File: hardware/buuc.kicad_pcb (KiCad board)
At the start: 2 copper layers, 45.1 x 29.8 mm, 15 parts, among them P1 USB_OTG, P2 CONN_01X02, Q1 NDS8434, U1 BOOST_REGULATOR, U2 MCP73842-840I/UN

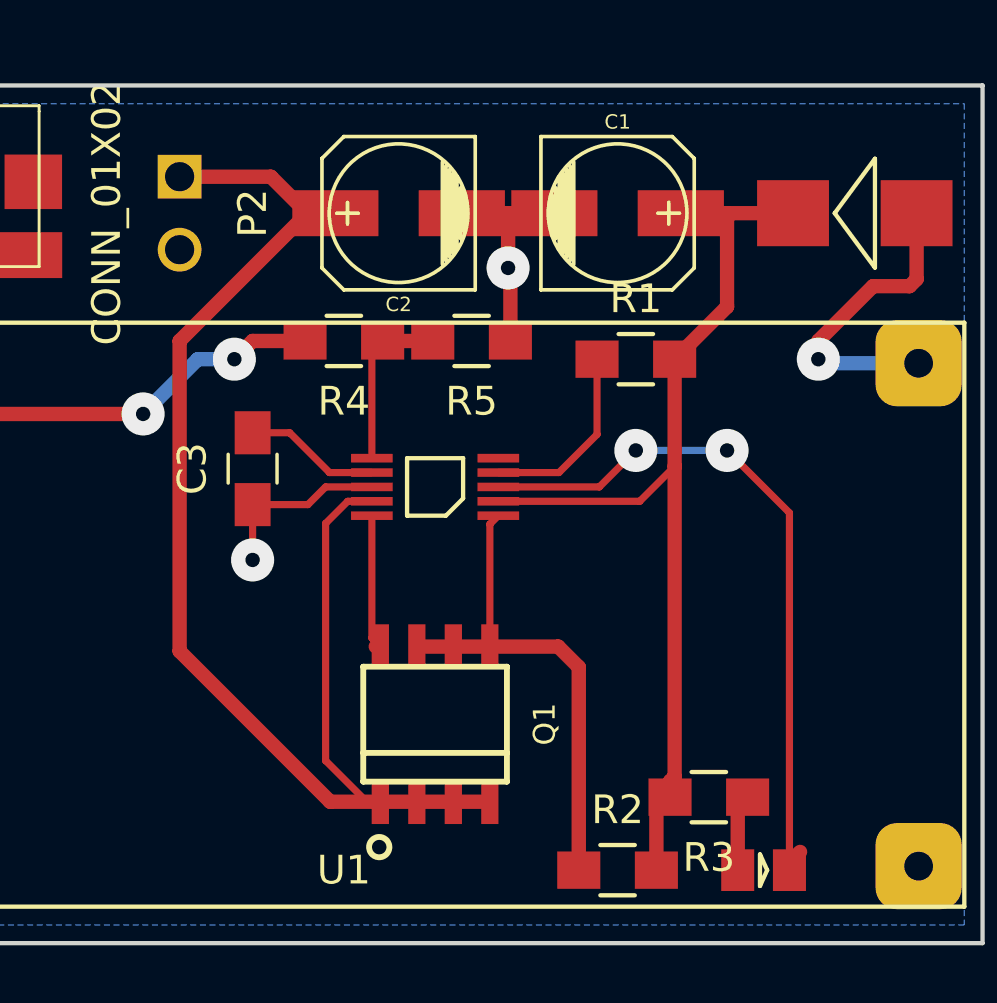
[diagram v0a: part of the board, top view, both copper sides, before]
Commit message: Updating schematics.
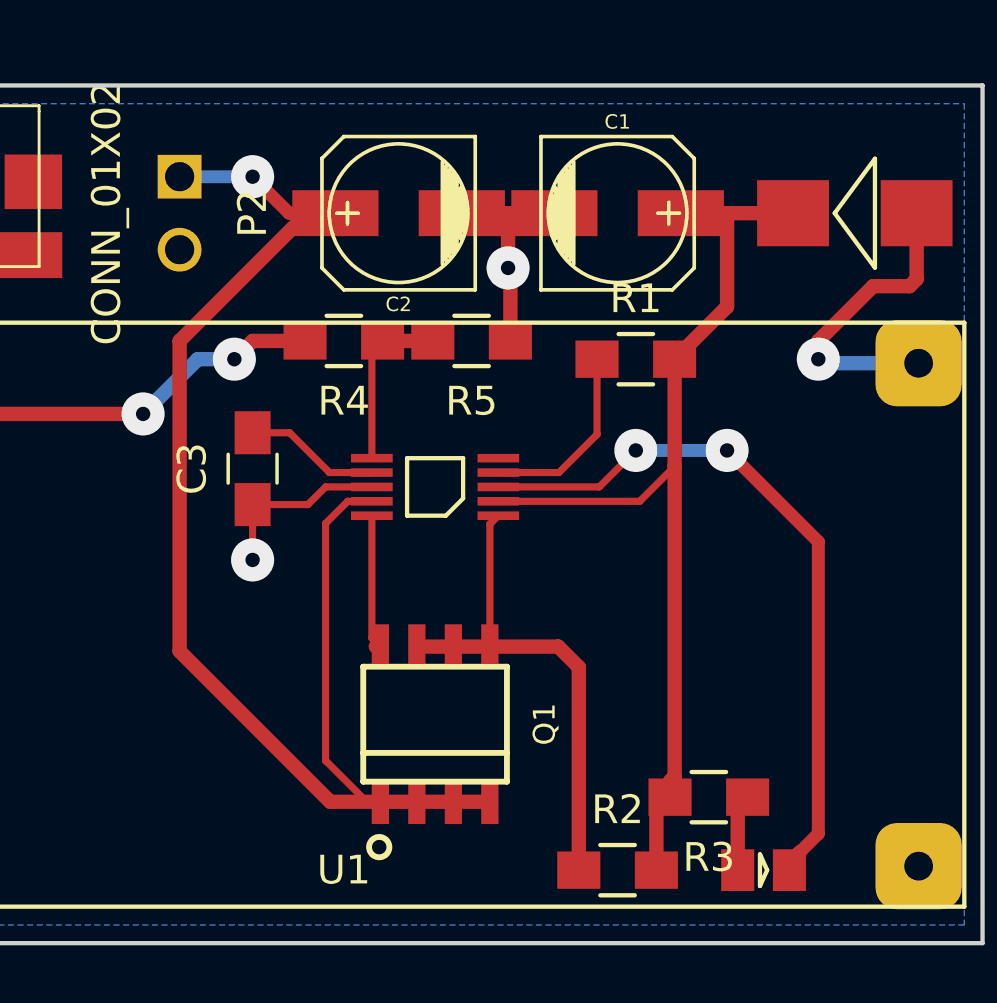
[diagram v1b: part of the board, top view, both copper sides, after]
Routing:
- net +BATT: track 49.6 -> 50.6 mm, vias 0 -> 1
- net Net-(D2-Pad1): track 24.8 -> 25.3 mm
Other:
- net class Default: trace_width 0.25 -> 0.45

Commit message: Adding MIC2005 current limiting IC; I haven't even soldered everything together, but it's pretty clear this will be necessary.
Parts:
- added C4: 0.1u, KiCad/Capacitors_SMD.pretty:C_0805_HandSoldering, F.Cu at (59.1, 48.3)
- added R6: 10k, apexelectrix/apex-smd-resistors.pretty:R_0805_HandSoldering, F.Cu at (57.1, 45.7)
- added U3: MIC2005A, adamgreig/agg-kicad/agg.pretty:SOT-23-6, F.Cu at (57.1, 54.0)
- moved C1 90.5 mm to (79.4, 38.7)
- moved C2 90.5 mm to (71.8, 38.7)
- moved D1 90.5 mm to (87.6, 38.7)
- moved P1 90.5 mm to (55.2, 36.2)
- moved Q1 90.5 mm to (73.0, 56.5)
- moved R2 90.5 mm to (79.4, 61.6)
- moved R4 90.5 mm to (69.8, 43.2)
- moved U1 90.5 mm to (69.8, 52.7)
- moved U2 90.5 mm to (73.0, 48.3)
- moved C3 90.5 mm to (66.7, 47.6)
- moved D2 90.5 mm to (84.5, 61.6)
- moved P2 90.5 mm to (64.1, 38.7)
- moved R1 90.5 mm to (80.0, 43.8)
- moved R3 90.5 mm to (82.5, 59.1)
- moved R5 90.5 mm to (74.3, 43.2)
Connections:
- P1 pad 1: +5V -> Net-(C4-Pad2)
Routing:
- net +5V: track 24.0 -> 43.5 mm
- net Net-(C4-Pad2): track 0.00 -> 17.7 mm
- net Net-(R6-Pad2): track 0.00 -> 7.12 mm
- net GND: track 17.5 -> 21.5 mm, vias 3 -> 4

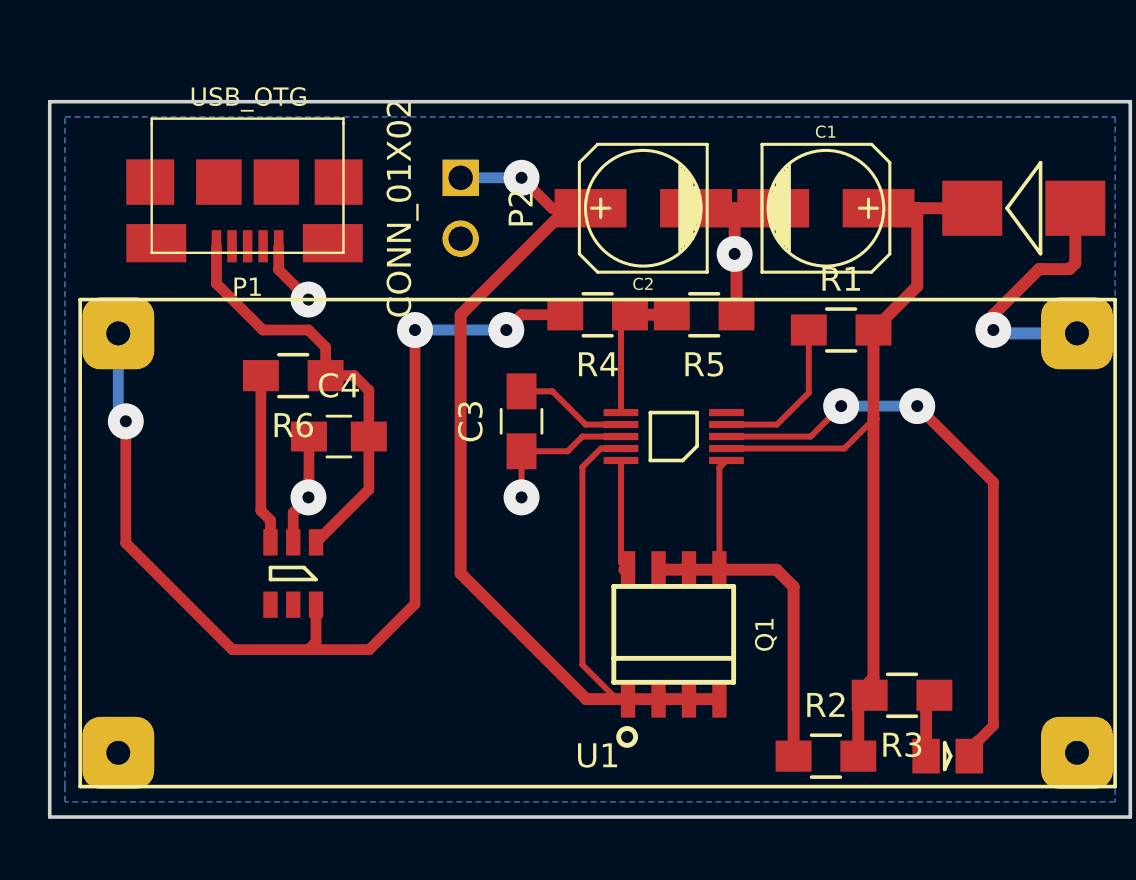
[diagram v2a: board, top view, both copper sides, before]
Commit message: Swapping resistor footprint for one that's a bit easier to solder onto a milled board; minor move of the USB connector.
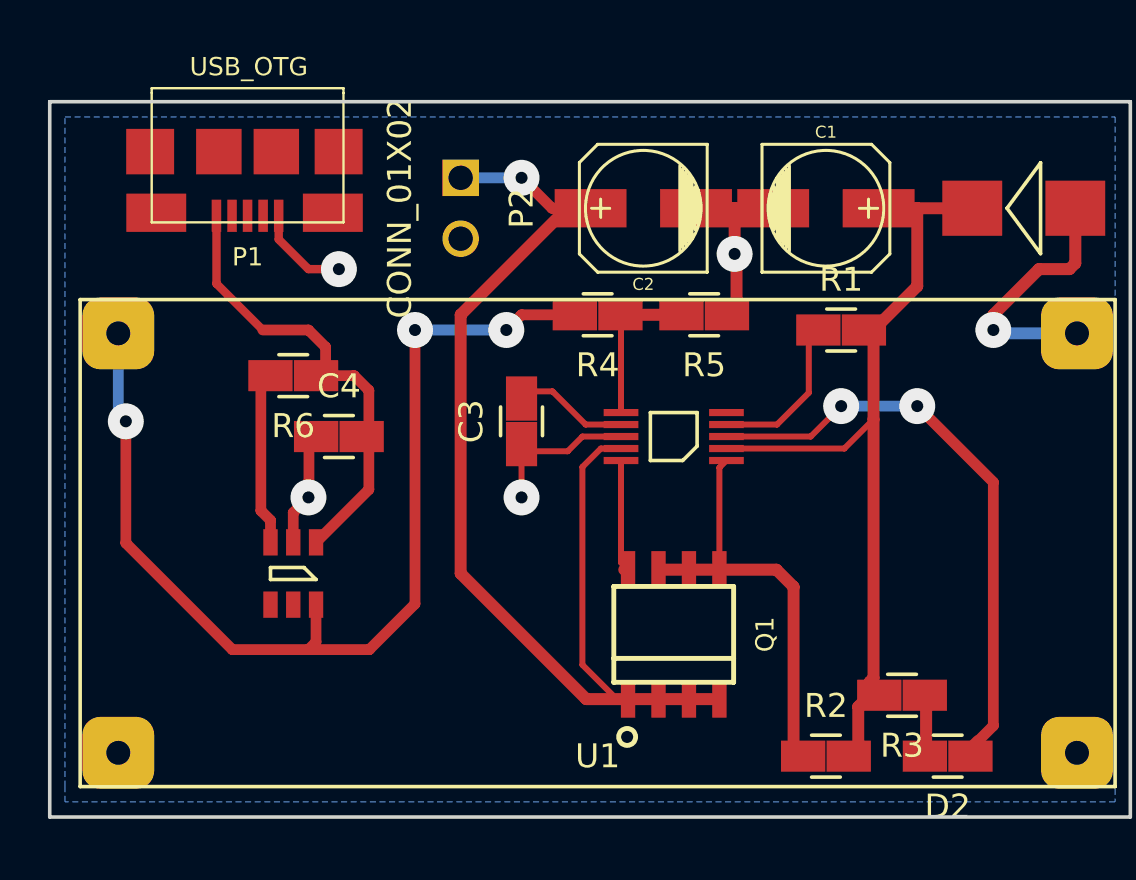
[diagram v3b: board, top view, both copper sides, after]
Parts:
- C3, C4: footprint KiCad/Capacitors_SMD.pretty:C_0805_HandSoldering -> coddingtonbear/coddingtonbear.pretty:0805_Milling
- D2: footprint adamgreig/agg-kicad/agg.pretty:0805-LED -> coddingtonbear/coddingtonbear.pretty:0805_Milling
- R1, R2, R3, R6: footprint apexelectrix/apex-smd-resistors.pretty:R_0805_HandSoldering -> coddingtonbear/coddingtonbear.pretty:0805_Milling
- R4: value 1k -> 33k; footprint apexelectrix/apex-smd-resistors.pretty:R_0805_HandSoldering -> coddingtonbear/coddingtonbear.pretty:0805_Milling
- R5: value 200 -> 6.8k; footprint apexelectrix/apex-smd-resistors.pretty:R_0805_HandSoldering -> coddingtonbear/coddingtonbear.pretty:0805_Milling
- moved P1 1.27 mm to (55.2, 34.9)
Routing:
- net Net-(C4-Pad2): track 17.7 -> 19.0 mm
- net GND: track 21.5 -> 22.7 mm
